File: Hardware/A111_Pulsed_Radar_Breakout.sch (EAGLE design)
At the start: 26 parts, among them J4 RASPBERRYPI-26-PIN-GPIO, U1 A111, U2 1.8V, U4 TXB0108DQSR, Y1 26MHz

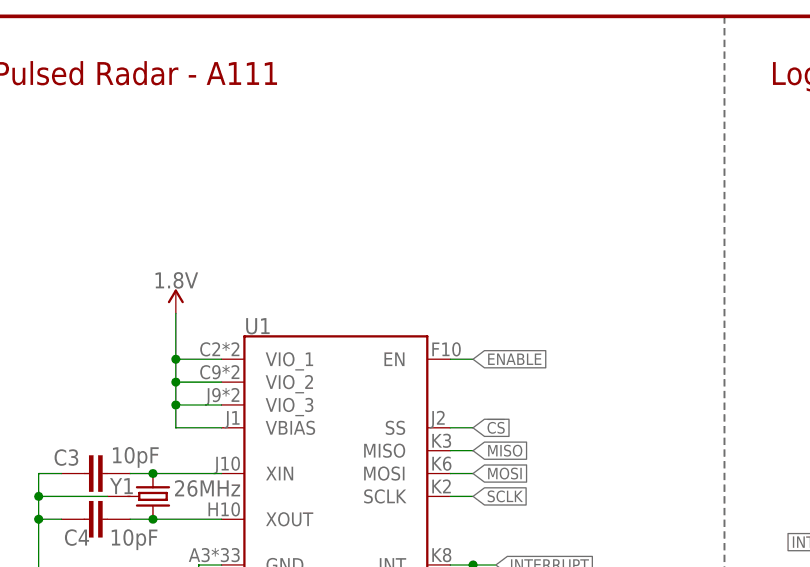
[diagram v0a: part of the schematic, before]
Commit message: Updates schematic with VCC range, updates silk on A111 part
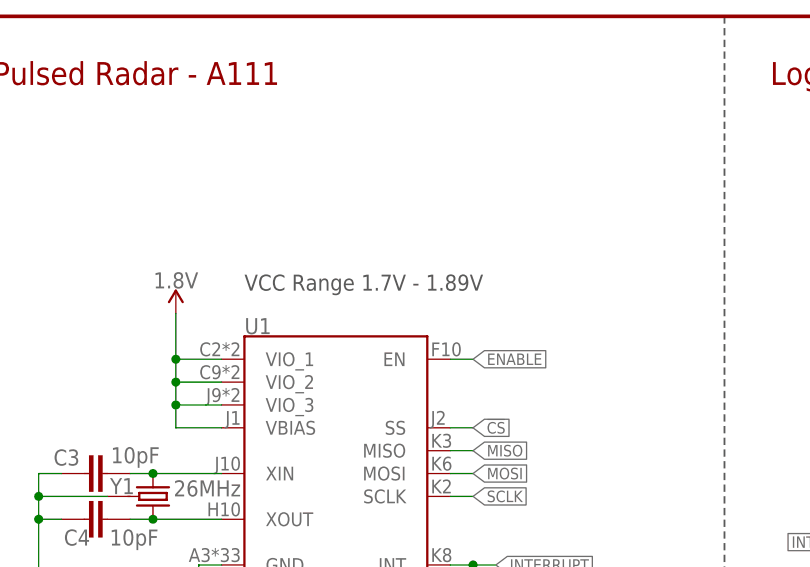
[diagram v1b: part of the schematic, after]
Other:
- note added: "VCC Range 1.7V - 1.89V"
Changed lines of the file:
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@@
 <?xml version="1.0" encoding="utf-8"?>
 <!DOCTYPE eagle SYSTEM "eagle.dtd">
-<eagle version="9.4.2">
+<eagle version="9.4.0">
 <drawing>
 <settings>
@@
 <text x="167.64" y="127" size="2.54" layer="94" font="vector">Voltage Regulator </text>
 <text x="30.48" y="10.16" size="1.27" layer="97" font="vector">40 pin is backwards compatible with 26 pin header.</text>
+<text x="33.02" y="154.94" size="1.778" layer="97" font="vector">VCC Range 1.7V - 1.89V</text>
 </plain>
 <instances>
